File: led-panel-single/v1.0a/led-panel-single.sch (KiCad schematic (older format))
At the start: 22 parts, among them J1 5V, J2 jmp, J3 Conn_02x08_Odd_Even, J4 PMOD, J5 jmp, U1 SN74LVC8T245, U2 NL27WZ14, U3 74HC4024, U4 74VHC574

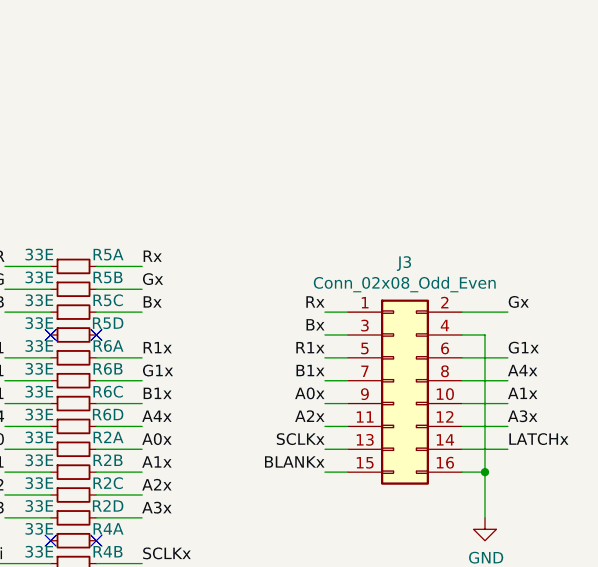
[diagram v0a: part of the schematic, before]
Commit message: Placement plan improvements.
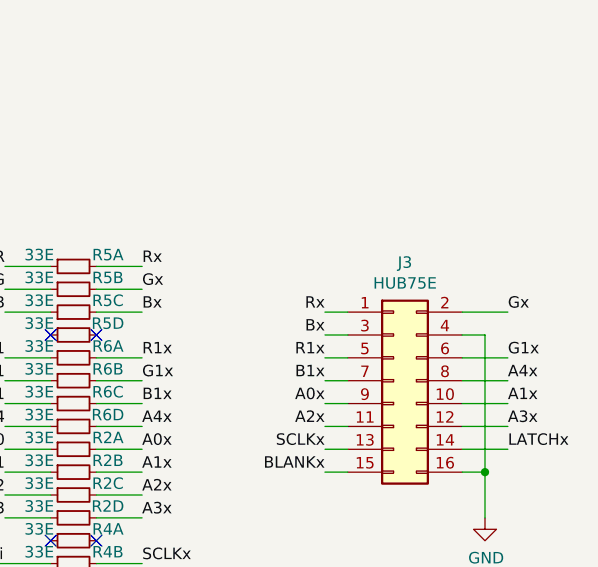
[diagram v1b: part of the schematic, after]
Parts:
- J3: value Conn_02x08_Odd_Even -> HUB75E
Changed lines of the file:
@@
 P 9100 3500
 F 0 "J3" H 9150 4017 50  0000 C CNN
-F 1 "Conn_02x08_Odd_Even" H 9150 3926 50  0000 C CNN
+F 1 "HUB75E" H 9150 3926 50  0000 C CNN
 F 2 "Connector_IDC:IDC-Header_2x08_P2.54mm_Vertical" H 9100 3500 50  0001 C CNN
 F 3 "~" H 9100 3500 50  0001 C CNN

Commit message: Some global cleanup.
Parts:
- U3: value 74HC4024 -> CD74HC4024PWR
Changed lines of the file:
@@
 EESchema Schematic File Version 4
 LIBS:led-panel-single-cache
-EELAYER 26 0
+EELAYER 29 0
 EELAYER END
 $Descr A4 11693 8268
@@
 P 6000 4600
 F 0 "U3" H 6000 5170 50  0000 C CNN
-F 1 "74HC4024" H 6000 5077 50  0000 C CNN
+F 1 "CD74HC4024PWR" H 6000 5077 50  0000 C CNN
 F 2 "Package_SO:TSSOP-14_4.4x5mm_P0.65mm" H 6050 5700 50  0001 C CNN
 F 3 "" H 6050 5700 50  0001 C CNN
